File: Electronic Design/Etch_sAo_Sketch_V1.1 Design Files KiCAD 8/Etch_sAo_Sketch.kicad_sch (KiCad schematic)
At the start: 17 parts, among them U1 LIS3DHTR, X1 SAO_conn_SFH11-NBPC-D03-ST-BK, X2 OLED_128x128

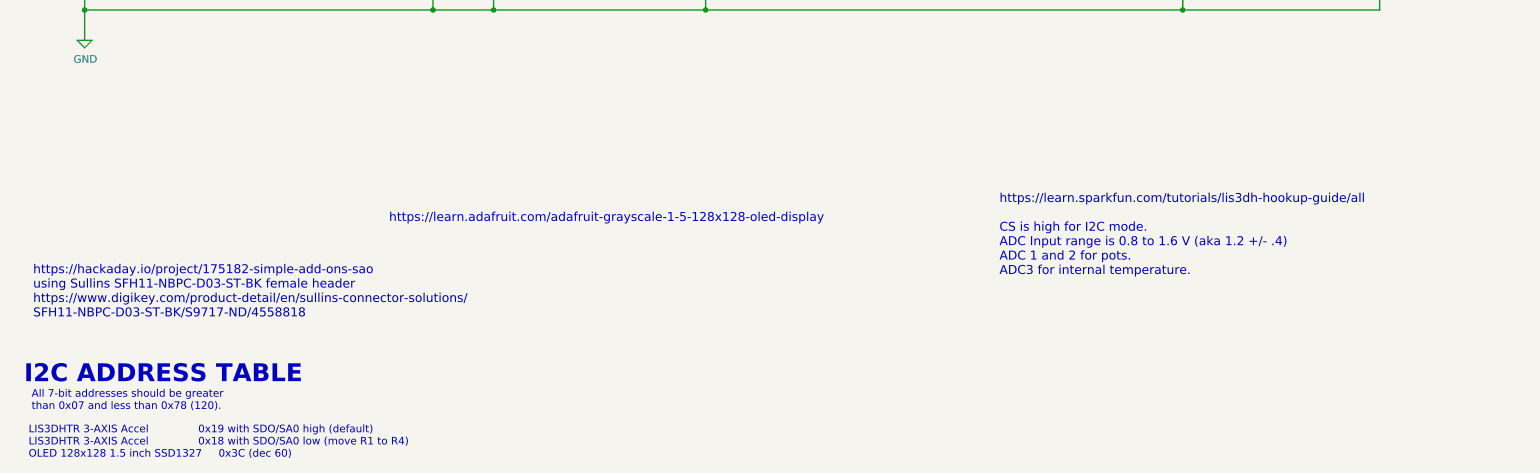
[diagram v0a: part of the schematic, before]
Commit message: Update schematic notes V1.1, add manufacturing verification images
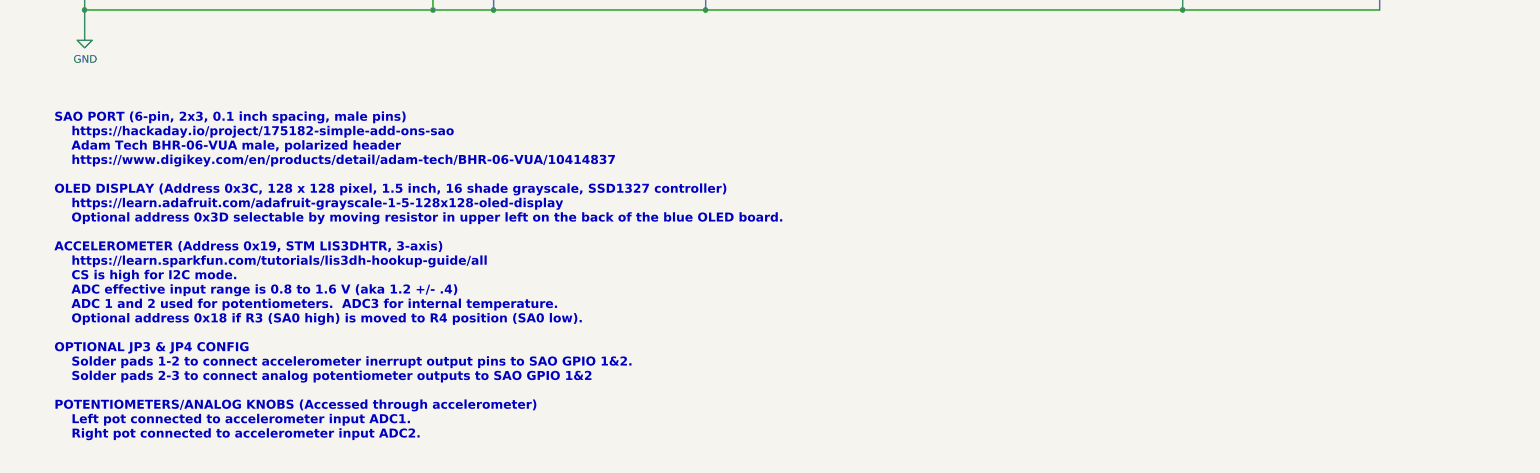
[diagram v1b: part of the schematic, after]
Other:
- note added: "SAO PORT (6-pin, 2x3, 0.1 inch spacing, male pins) https://hackaday.io/project/175182-simple-add-ons-sao Adam Tech BHR-06-VUA male, polarized header https://www.digikey.com/en/products/detail/adam-tech/BHR-06-VUA/10414837 OLED DISPLAY (Address 0x3C, 128 x 128 pixel, 1.5 inch, 16 shade grayscale, SSD1327 controller) https://learn.adafruit.com/adafruit-grayscale-1-5-128x128-oled-display Optional ad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"
- note removed: "All 7-bit addresses should be greater than 0x07 and less than 0x78 (120)."
- note removed: "I2C ADDRESS TABLE"
- note removed: "LIS3DHTR 3-AXIS Accel 0x19 with SDO/SA0 high (default) LIS3DHTR 3-AXIS Accel 0x18 with SDO/SA0 low (move R1 to R4) OLED 128x128 1.5 inch SSD1327 0x3C (dec 60)"
- note removed: "https://hackaday.io/project/175182-simple-add-ons-sao using Sullins SFH11-NBPC-D03-ST-BK female header https://www.digikey.com/product-detail/en/sullins-connector-solutions/ SFH11-NBPC-D03-ST-BK/S9717-ND/4558818"
- note removed: "https://learn.adafruit.com/adafruit-grayscale-1-5-128x128-oled-display"
- note removed: "https://learn.sparkfun.com/tutorials/lis3dh-hookup-guide/all CS is high for I2C mode. ADC Input range is 0.8 to 1.6 V (aka 1.2 +/- .4) ADC 1 and 2 for pots. ADC3 for internal temperature."
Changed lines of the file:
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@@
 		)
 	)
-	(text "https://hackaday.io/project/175182-simple-add-ons-sao\nusing Sullins SFH11-NBPC-D03-ST-BK female header\nhttps://www.digikey.com/product-detail/en/sullins-connector-solutions/\nSFH11-NBPC-D03-ST-BK/S9717-ND/4558818"
+	(text "SAO PORT (6-pin, 2x3, 0.1 inch spacing, male pins)\n    https://hackaday.io/project/175182-simple-add-ons-sao\n    Adam Tech BHR-06-VUA male, polarized header\n    https://www.digikey.com/en/products/detail/adam-tech/BHR-06-VUA/10414837\n\nOLED DISPLAY (Address 0x3C, 128 x 128 pixel, 1.5 inch, 16 shade grayscale, SSD1327 controller)\n    https://learn.adafruit.com/adafruit-grayscale-1-5-128x128-oled-display\n    Optional address 0x3D selectable by moving resistor in upper left on the back of the blue OLED board.\n\nACCELEROMETER (Address 0x19, STM LIS3DHTR, 3-axis)\n    https://learn.sparkfun.com/tutorials/lis3dh-hookup-guide/all\n    CS is high for I2C mode.\n    ADC effective input range is 0.8 to 1.6 V (aka 1.2 +/- .4)\n    ADC 1 and 2 used for potentiometers.  ADC3 for internal temperature.\n    Optional address 0x18 if R3 (SA0 high) is moved to R4 position (SA0 low).\n\nOPTIONAL JP3 & JP4 CONFIG\n    Solder pads 1-2 to connect accelerometer inerrupt output pins to SAO GPIO 1&2.\n    Solder pads 2-3 to connect analog potentiometer outputs to SAO GPIO 1&2  \n\nPOTENTIOMETERS/ANALOG KNOBS (Accessed through accelerometer)\n    Left pot connected to accelerometer input ADC1.\n    Right pot connected to accelerometer input ADC2."
 		(exclude_from_sim no)
-		(at 16.764 176.276 0)
+		(at 20.32 196.596 0)
 		(effects
 			(font
 				(size 1.5 1.5)
-			)
-			(justify left bottom)
-		)
-	)
-	(text "https://learn.adafruit.com/adafruit-grayscale-1-5-128x128-oled-display"
-		(exclude_from_sim no)
-		(at 76.454 160.274 0)
-		(effects
-			(font
-				(size 1.5 1.5)
-			)
-			(justify left bottom)
-		)
-	)
-	(text "LIS3DHTR 3-AXIS Accel               0x19 with SDO/SA0 high (default)\nLIS3DHTR 3-AXIS Accel               0x18 with SDO/SA0 low (move R1 to R4)\nOLED 128x128 1.5 inch SSD1327     0x3C (dec 60)"
-		(exclude_from_sim no)
-		(at 16.002 199.771 0)
-		(effects
-			(font
-				(size 1.27 1.27)
+				(thickness 0.3)
+				(bold yes)
 			)
 			(justify left bottom)
@@
 		)
 	)
-	(text "https://learn.sparkfun.com/tutorials/lis3dh-hookup-guide/all\n\nCS is high for I2C mode.\nADC Input range is 0.8 to 1.6 V (aka 1.2 +/- .4)\nADC 1 and 2 for pots.\nADC3 for internal temperature."
-		(exclude_from_sim no)
-		(at 178.816 169.164 0)
-		(effects
-			(font
-				(size 1.5 1.5)
-			)
-			(justify left bottom)
-		)
-	)
 	(text "ETCH sAo SKETCH - OLED VERSION"
 		(exclude_from_sim no)
@@
 		)
 	)
-	(text "I2C ADDRESS TABLE"
-		(exclude_from_sim no)
-		(at 15.24 187.325 0)
-		(effects
-			(font
-				(size 2.9972 2.9972)
-				(thickness 0.5994)
-				(bold yes)
-			)
-			(justify left bottom)
-		)
-	)
 	(text "ACCELEROMETER"
 		(exclude_from_sim no)
@@
 			)
 			(justify left bottom)
-		)
-	)
-	(text "All 7-bit addresses should be greater\nthan 0x07 and less than 0x78 (120)."
-		(exclude_from_sim no)
-		(at 16.51 191.77 0)
-		(effects
-			(font
-				(size 1.27 1.27)
-			)
-			(justify left bottom)

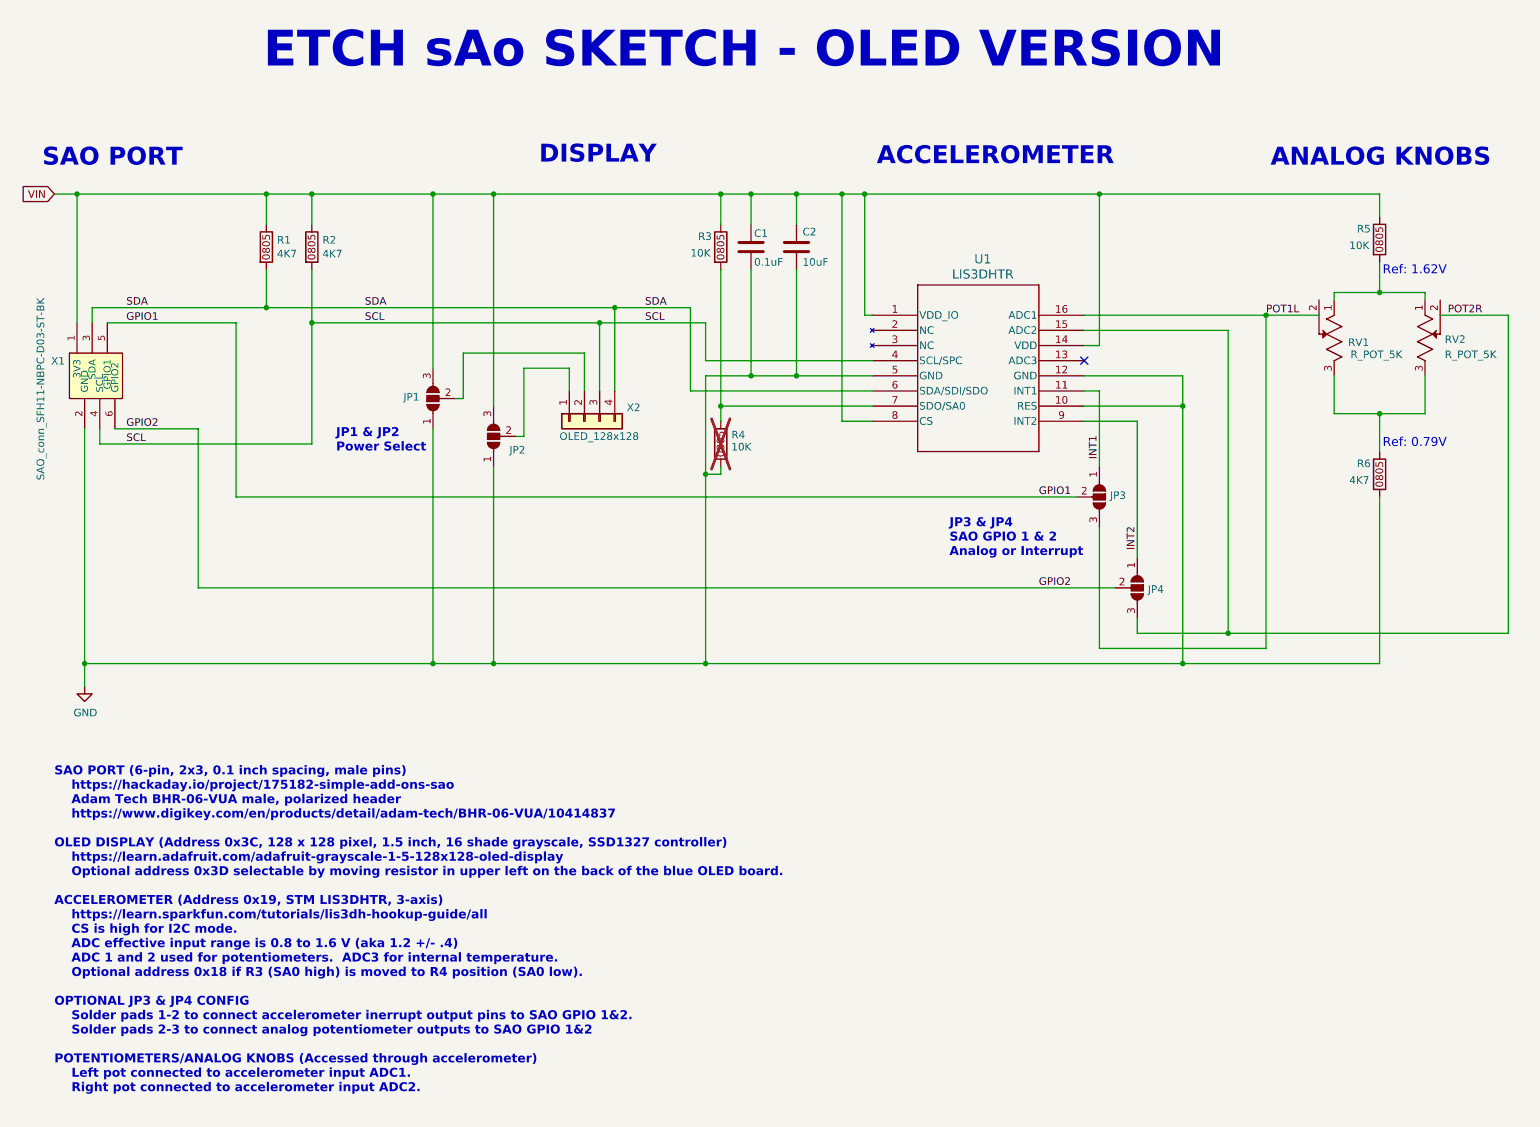
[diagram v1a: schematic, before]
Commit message: Hardware V1.1 schematic and firmware test updated
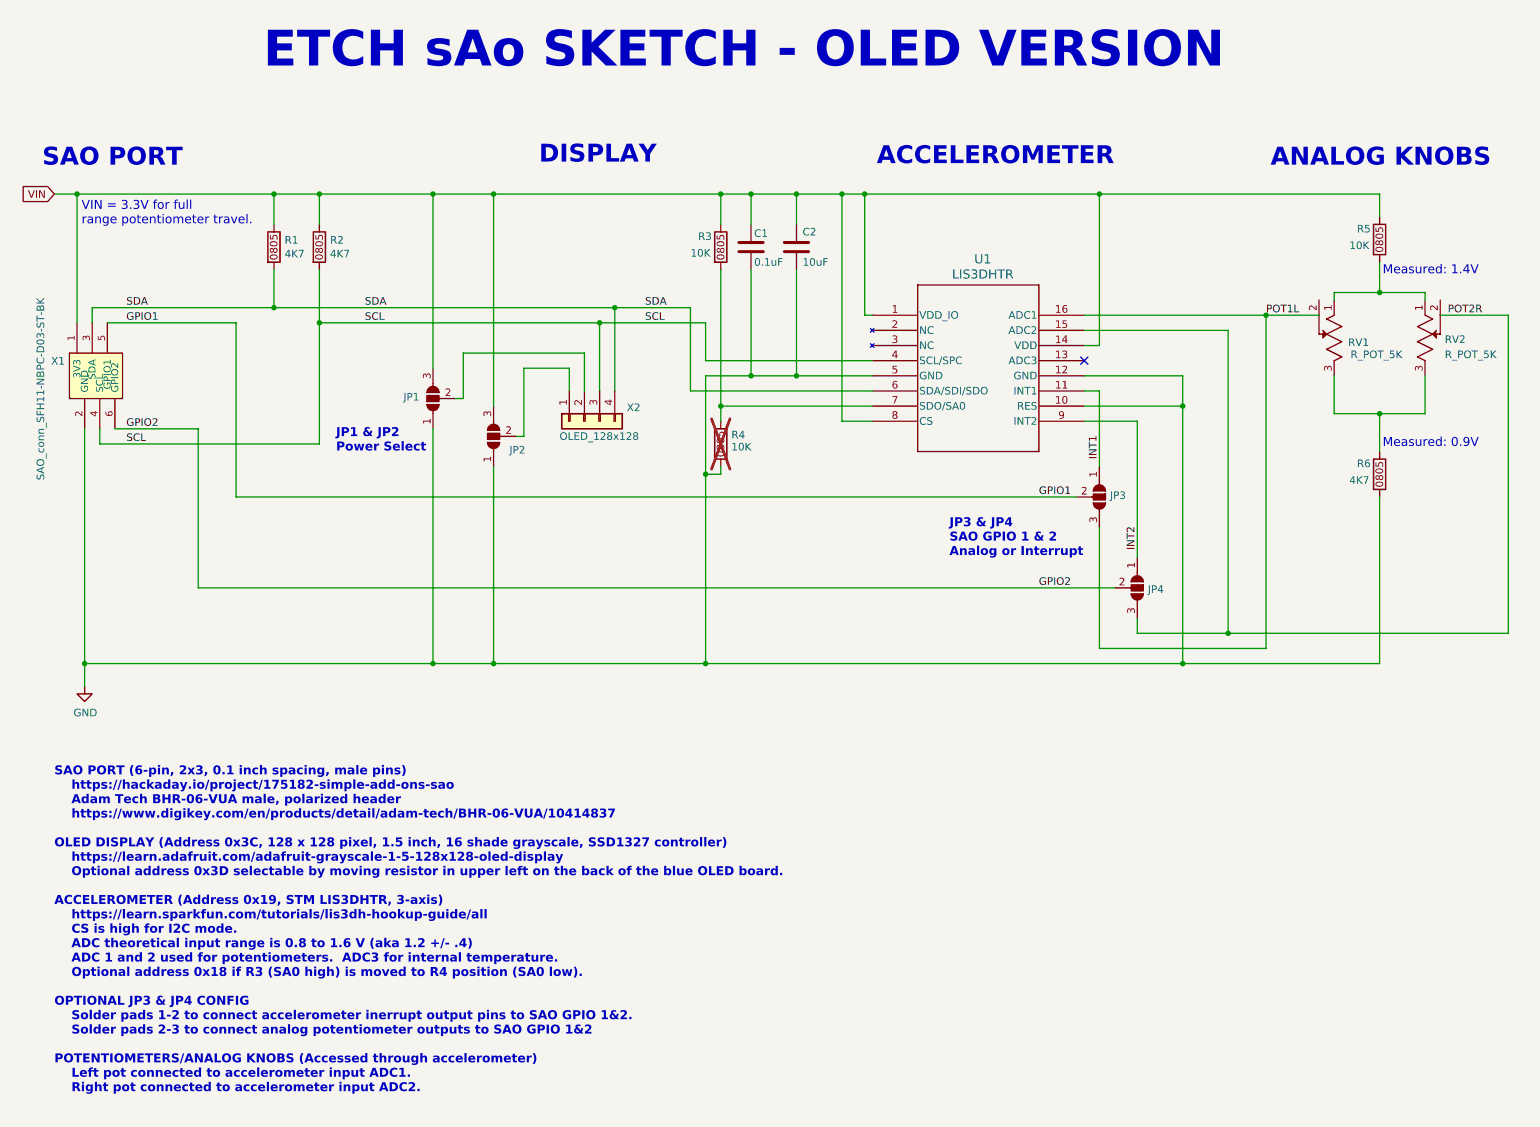
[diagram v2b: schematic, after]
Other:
- note added: "Measured: 0.9V"
- note added: "Measured: 1.4V"
- note added: "VIN = 3.3V for full range potentiometer travel."
- note removed: "Ref: 0.79V"
- note removed: "Ref: 1.62V"
- moved on the sheet: R1, R2
